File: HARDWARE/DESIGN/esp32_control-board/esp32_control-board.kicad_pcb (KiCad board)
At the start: 2 copper layers, 120 x 85 mm, 148 parts, among them J101 Power-in, J201 RFID-module1, J204 USB-prog, J4 Termination, J401 CAN, J402 I2C, J403 UART, J405 Din1, J406 Din3, J407 Din2, J408 Din4, J409 Lock1, J410 Lock2, J411 Ain2, J412 Ain1, Q102 DMP3013SFV-7, Q401 AO3401A, Q402 BSS138, Q403 BSS138, Q404 AO3401A, Q405 BSS138, Q406 DMP6180SK3-13, SW201 Boot, SW202 Reset, U101 LM63615DQDRRRQ1, U102 AMS1117-3.3, U203 ESP32-S3-WROOM-1U, U204 USBLC6-2SC6, U205 USBLC6-2SC6, U401 SN74LVC125ADR, U409 PC817, U410 PC817, U411 PC817, U412 PC817, U6 TCAN330

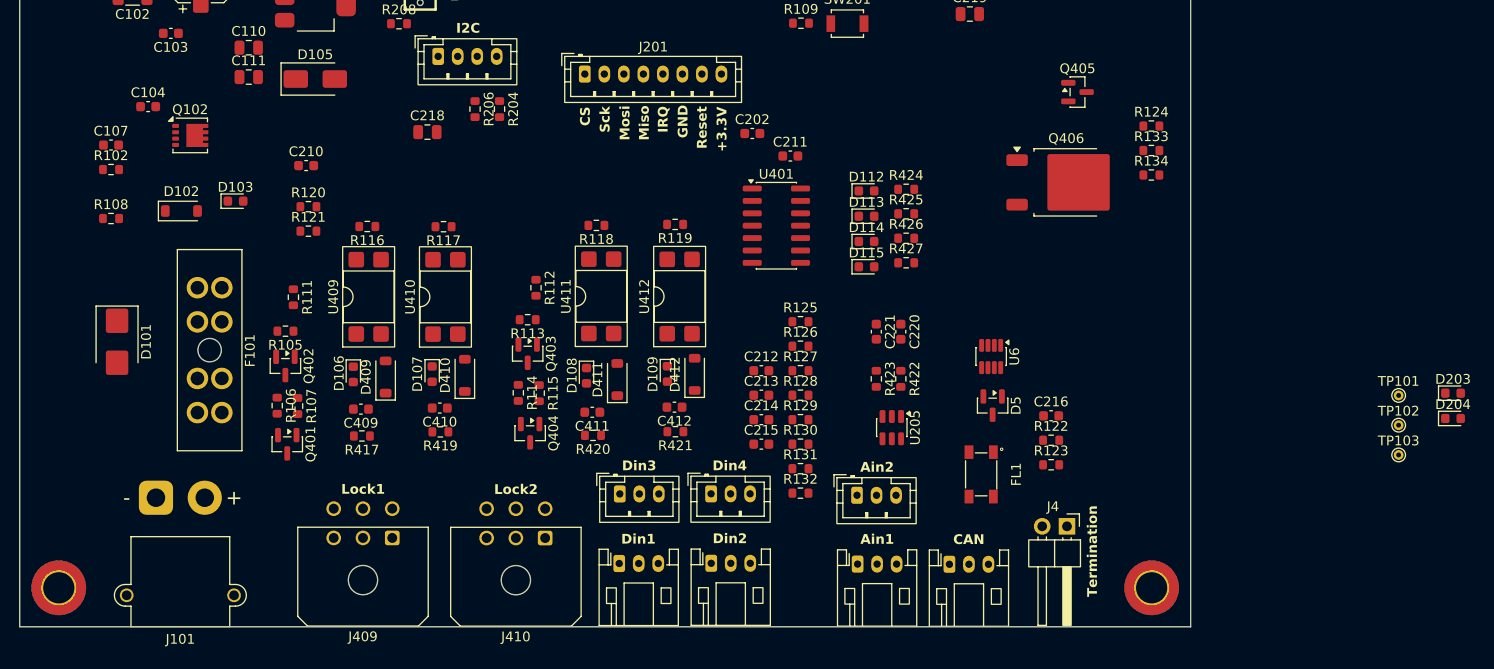
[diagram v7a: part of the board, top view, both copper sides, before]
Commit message: 60905 - fuse-holder replaced, led-strip connector added
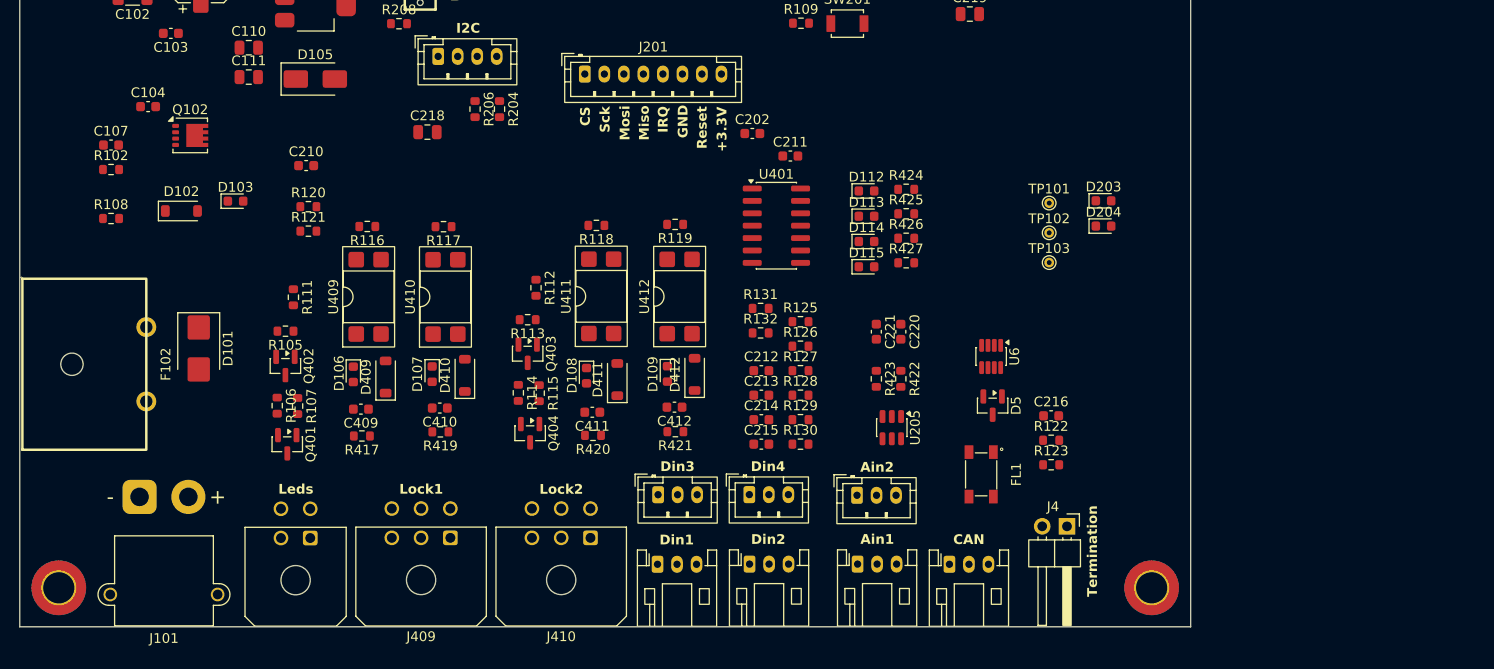
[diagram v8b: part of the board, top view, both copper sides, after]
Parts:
- removed F101: XF-087, Fuse:FuseHolder_Blade_ATO_Littelfuse_FLR_178.6165
- removed Q405: BSS138, Package_TO_SOT_SMD:SOT-23
- removed Q406: DMP6180SK3-13, Package_TO_SOT_SMD:TO-252-2
- removed R124: 120, Resistor_SMD:R_0603_1608Metric
- removed R133, R134: 12k, Resistor_SMD:R_0603_1608Metric
- added F102: XF-087, (FOOTPRINTS):C206906_LittleFuse_01530007Z, F.Cu at (83.2, 128.0)
- added J413: Leds, Connector_Molex:Molex_Micro-Fit_3.0_43045-0400_2x02_P3.00mm_Horizontal, F.Cu at (100.0, 145.8)
- moved D203 40.9 mm to (181.3, 111.2)
- moved D204 40.9 mm to (181.3, 113.8)
- moved TP101 40.9 mm to (175.7, 111.5)
- moved TP102 40.9 mm to (175.7, 114.5)
- moved TP103 40.9 mm to (175.7, 117.6)
- moved R132 16.9 mm to (146.2, 124.8)
- moved R131 16.9 mm to (146.2, 122.3)
- moved D101 8.40 mm to (88.6, 126.4)
- moved J409 5.96 mm to (114.4, 145.8)
- moved J410 4.65 mm to (128.7, 145.8)
- moved J405 3.93 mm to (135.6, 148.5)
- moved J408 3.93 mm to (145.0, 141.4)
- moved J406 3.93 mm to (135.7, 141.4)
- moved J407 3.93 mm to (145.0, 148.5)
- moved J101 1.68 mm to (82.5, 141.6)
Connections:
- J101 pad 1: GND -> +12V-in
- J101 pad 2: +12V-in -> GND
